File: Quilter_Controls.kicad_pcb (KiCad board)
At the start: 2 copper layers, 40.4 x 110 mm, 18 parts, among them J1 Conn_01x10_Male, J10 Conn_01x04_Male, J11 Freq_In, J2 Conn_01x10_Male, J3 Conn_01x10_Male, J4 Audio_In, J5 Audio_Out, J6 Audio_Mix, J7 Freq_V_Oct, J8 Freq_CV_Damp, J9 Conn_02x04_Top_Bottom

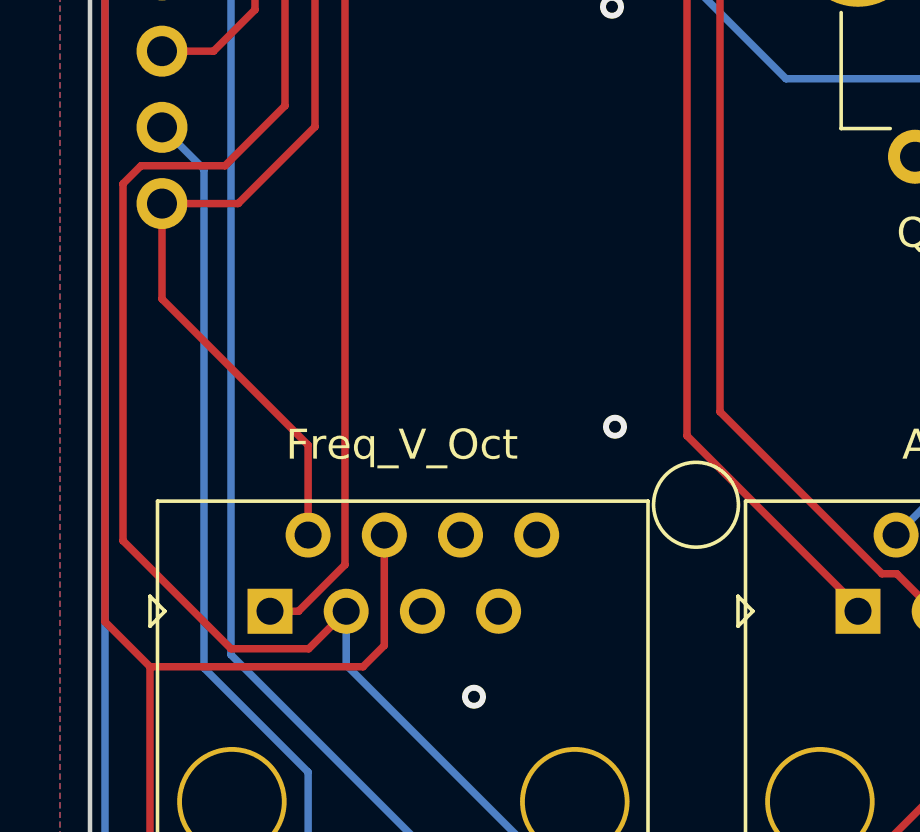
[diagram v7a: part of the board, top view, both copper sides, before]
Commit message: Prepared v2 Controls and Components for manufacture
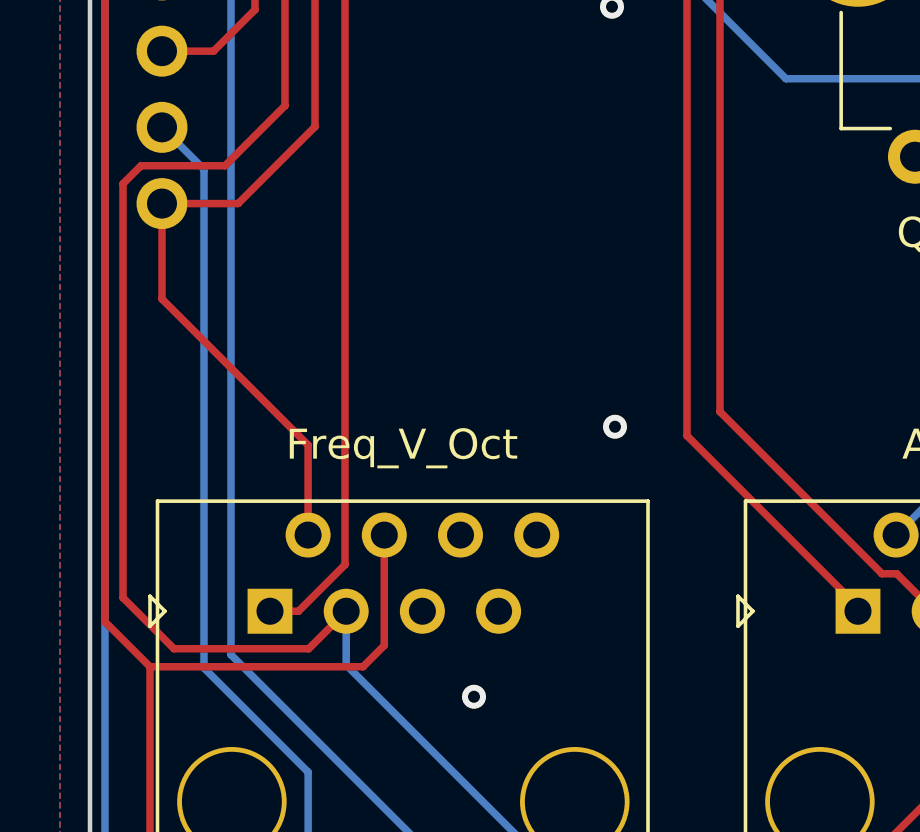
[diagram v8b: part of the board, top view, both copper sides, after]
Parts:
- removed D1: 3d_Model_Components, Custom_Footprints:3D_Dummy
- removed D2: 3d_Model_Panel, Custom_Footprints:3D_Dummy
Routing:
- net /FREQ_V_OCT3: track 128.5 -> 129.7 mm
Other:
- board text added: "Aud In"
- board text removed: "In"
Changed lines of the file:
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@@
     (pad_to_mask_clearance 0)
     (pcbplotparams
-      (layerselection 0x00010fc_ffffffff)
+      (layerselection 0x00010f0_ffffffff)
       (disableapertmacros false)
       (usegerberextensions false)
@@
       (drillshape 0)
       (scaleselection 1)
-      (outputdirectory "Gerbers/Controls/")
+      (outputdirectory "Gerbers/Quilter_Controls/")
     )
   )
@@
   (net 40 "+12V")
   (net 41 "/FREQ_POT_-5V")
-  (footprint "Custom_Footprints:3D_Dummy" (layer "F.Cu")
-    (at 70.2 95.7)
-    (property "Sheetfile" "Quilter_Controls.kicad_sch")
-    (property "Sheetname" "")
-    (attr smd)
-    (fp_text reference "D2" (at 0 -0.5 unlocked) (layer "F.SilkS") hide
-      (effects (font (size 1 1) (thickness 0.15)))
-    )
-    (fp_text value "3d_Model_Panel" (at 0 -3 unlocked) (layer "F.Fab")
-      (effects (font (size 1 1) (thickness 0.15)))
-    )
-    (fp_text user "${REFERENCE}" (at 0 2.5 unlocked) (layer "F.Fab")
-      (effects (font (size 1 1) (thickness 0.15)))
-    )
-    (fp_circle (center 0 0) (end 1.414214 0) (layer "F.SilkS") (width 0.12) (fill none))
-    (model "${KIPRJMOD}/Graphics/Quilter_Panel.step" hide
-      (offset (xyz 0 0 10.5))
-      (scale (xyz 1 1 1))
-      (rotate (xyz 0 0 0))
-    )
-  )
   (footprint "Custom_Footprints:1.3mm_Test_Point" (layer "F.Cu")
     (at 70.2 42.97)
@@
     )
   )
-  (footprint "Custom_Footprints:3D_Dummy" (layer "B.Cu")
-    (at 70.2 100 180)
-    (property "Sheetfile" "Quilter_Controls.kicad_sch")
-    (property "Sheetname" "")
-    (attr smd)
-    (fp_text reference "D1" (at 0 0.5 unlocked) (layer "B.SilkS") hide
-      (effects (font (size 1 1) (thickness 0.15)) (justify mirror))
-    )
-    (fp_text value "3d_Model_Components" (at 0 3 unlocked) (layer "B.Fab")
-      (effects (font (size 1 1) (thickness 0.15)) (justify mirror))
-    )
-    (fp_text user "${REFERENCE}" (at 0 -2.5 unlocked) (layer "B.Fab")
-      (effects (font (size 1 1) (thickness 0.15)) (justify mirror))
-    )
-    (fp_circle (center 0 0) (end 1.414214 0) (layer "B.SilkS") (width 0.12) (fill none))
-    (model "${KIPRJMOD}/Graphics/Quilter_Components.step" hide
-      (offset (xyz 0 0 10))
-      (scale (xyz 1 1 1))
-      (rotate (xyz 0 0 0))
-    )
-  )
   (footprint "Connector_PinHeader_2.54mm:PinHeader_1x04_P2.54mm_Vertical" (layer "B.Cu")
     (at 87.8 43.7 90)
@@
     (effects (font (size 1.2 1.2) (thickness 0.2)) (justify mirror))
   )
-  (gr_text "In" (at 63.4 43.8) (layer "B.SilkS")
+  (gr_text "Aud In" (at 65.5 43.6) (layer "B.SilkS")
     (effects (font (size 1.2 1.2) (thickness 0.2)) (justify mirror))
   )
@@
   (segment (start 55.52 43.78) (end 56.9 42.4) (width 0.25) (layer "F.Cu") (net 21))
   (segment (start 56.9 42.4) (end 62.1 42.4) (width 0.25) (layer "F.Cu") (net 21))
+  (segment (start 55.52 46.375) (end 56.5 47.355) (width 0.25) (layer "F.Cu") (net 22))
+  (segment (start 52.8 100.5) (end 57.29 100.5) (width 0.25) (layer "F.Cu") (net 22))
+  (segment (start 54.5 84.4) (end 51.7 84.4) (width 0.25) (layer "F.Cu") (net 22))
+  (segment (start 56.5 82.4) (end 54.5 84.4) (width 0.25) (layer "F.Cu") (net 22))
+  (segment (start 56.5 47.355) (end 56.5 82.4) (width 0.25) (layer "F.Cu") (net 22))
+  (segment (start 51.1 85) (end 51.1 98.8) (width 0.25) (layer "F.Cu") (net 22))
   (segment (start 57.29 100.5) (end 58.54 99.25) (width 0.25) (layer "F.Cu") (net 22))
-  (segment (start 51.1 96.9) (end 54.7 100.5) (width 0.25) (layer "F.Cu") (net 22))
-  (segment (start 55.52 46.375) (end 56.5 47.355) (width 0.25) (layer "F.Cu") (net 22))
-  (segment (start 56.5 47.355) (end 56.5 82.4) (width 0.25) (layer "F.Cu") (net 22))
-  (segment (start 54.7 100.5) (end 57.29 100.5) (width 0.25) (layer "F.Cu") (net 22))
-  (segment (start 56.5 82.4) (end 54.5 84.4) (width 0.25) (layer "F.Cu") (net 22))
-  (segment (start 51.1 85) (end 51.1 96.9) (width 0.25) (layer "F.Cu") (net 22))
   (segment (start 51.7 84.4) (end 51.1 85) (width 0.25) (layer "F.Cu") (net 22))
-  (segment (start 54.5 84.4) (end 51.7 84.4) (width 0.25) (layer "F.Cu") (net 22))
+  (segment (start 51.1 98.8) (end 52.8 100.5) (width 0.25) (layer "F.Cu") (net 22))
   (segment (start 79 111.5) (end 69 111.5) (width 0.25) (layer "B.Cu") (net 22))
   (segment (start 80.7 113.2) (end 79 111.5) (width 0.25) (layer "B.Cu") (net 22))
